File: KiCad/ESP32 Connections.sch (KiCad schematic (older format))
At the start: 1 part

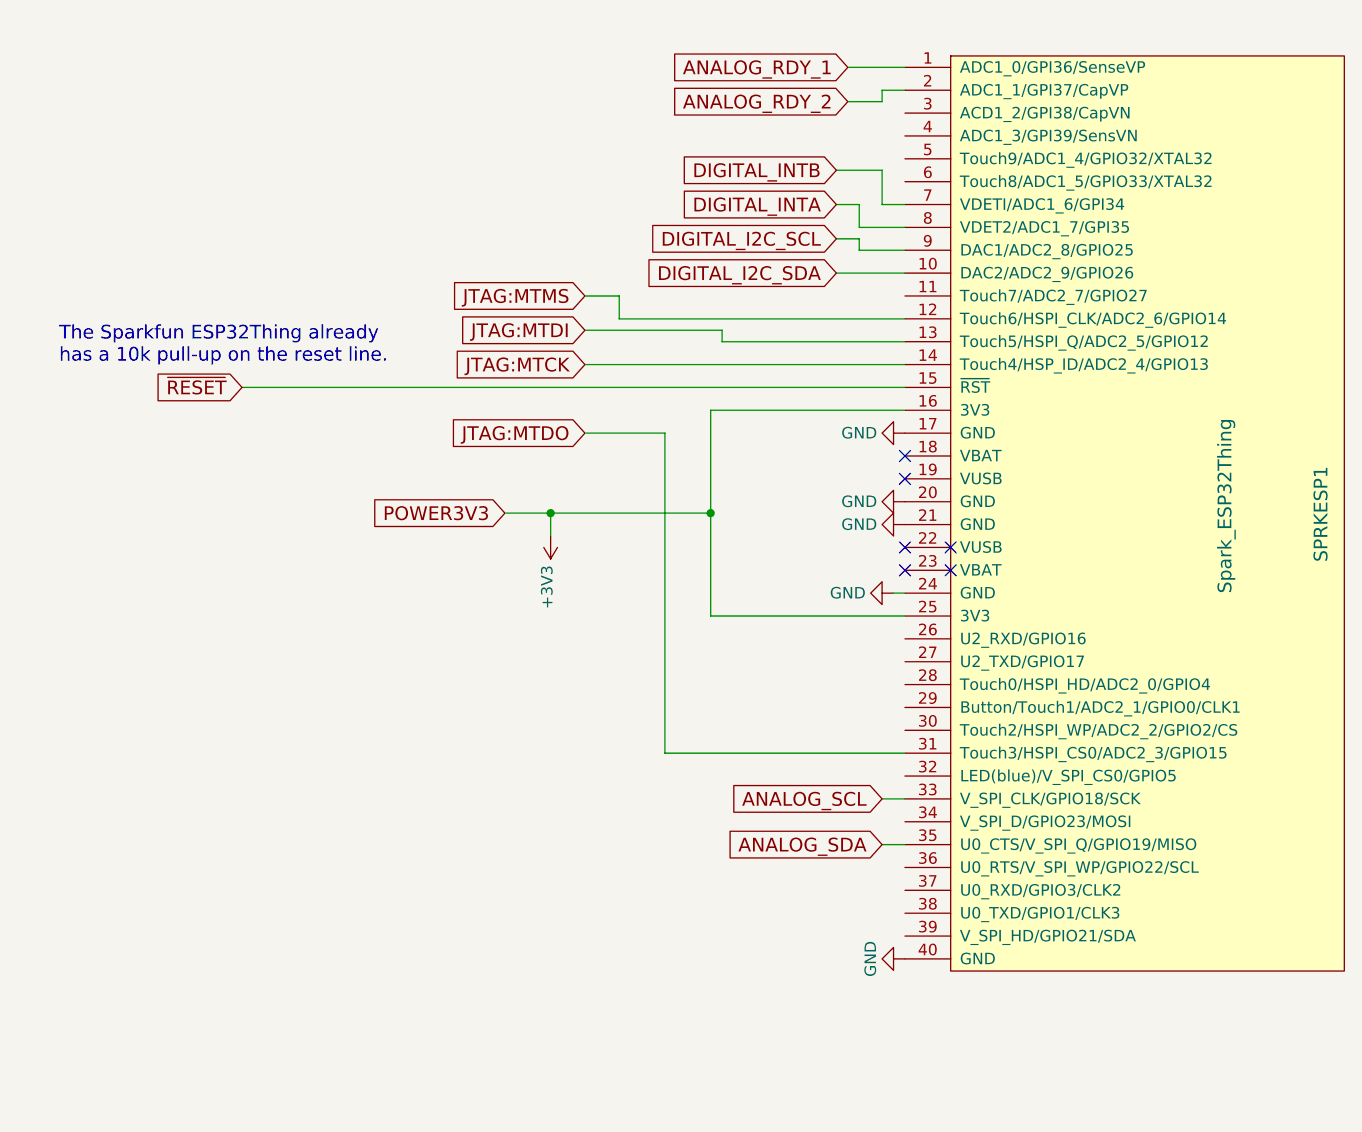
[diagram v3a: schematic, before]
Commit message: Reworked power-supply to provide 5V. Updated ESP-connections.
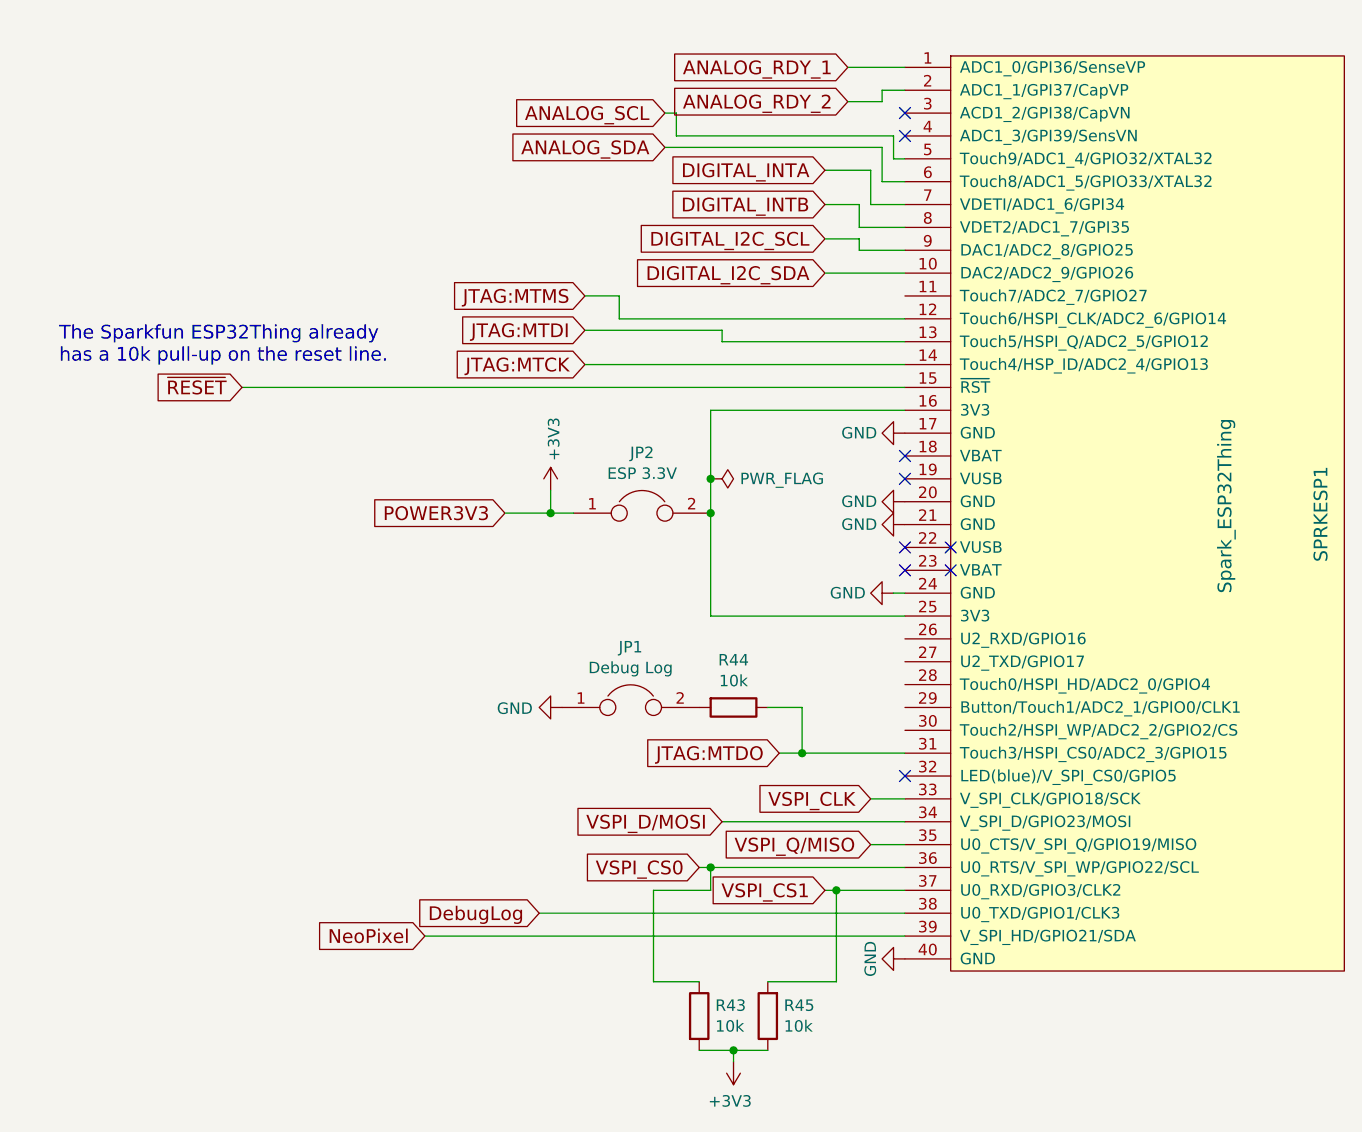
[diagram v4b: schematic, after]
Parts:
- added JP1: Debug Log, Pin_Headers:Pin_Header_Straight_1x02_Pitch2.54mm, symbol Jumper
- added JP2: ESP 3.3V, Pin_Headers:Pin_Header_Straight_1x02_Pitch2.54mm, symbol Jumper
- added R43, R44, R45: 10k, Resistors_SMD:R_0805, symbol R
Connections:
- net +3V3: now also JP2.1, R43.2, R45.1; no longer SPRKESP1.16 (3V3), SPRKESP1.25 (3V3)
- net ANALOG_SCL: now also SPRKESP1.5 (Touch9/ADC1_4/GPIO32/XTAL32); no longer SPRKESP1.33 (V_SPI_CLK/GPIO18/SCK)
- net ANALOG_SDA: now also SPRKESP1.6 (Touch8/ADC1_5/GPIO33/XTAL32); no longer SPRKESP1.35 (U0_CTS/V_SPI_Q/GPIO19/MISO)
- net DIGITAL_INTA: now also SPRKESP1.7 (VDETI/ADC1_6/GPI34); no longer SPRKESP1.8 (VDET2/ADC1_7/GPI35)
- net DIGITAL_INTB: now also SPRKESP1.8 (VDET2/ADC1_7/GPI35); no longer SPRKESP1.7 (VDETI/ADC1_6/GPI34)
- net GND: now also JP1.1
- net JTAG:MTDO: now also R44.1
- net VSPI_D/MOSI: now reaches SPRKESP1.34 (V_SPI_D/GPIO23/MOSI)
- net VSPI_CS0: now reaches SPRKESP1.36 (U0_RTS/V_SPI_WP/GPIO22/SCL)
- net VSPI_CS0: now also R43.1
- net VSPI_CS1: now reaches SPRKESP1.37 (U0_RXD/GPIO3/CLK2)
- net VSPI_CS1: now also R45.2
- net DebugLog: now reaches SPRKESP1.38 (U0_TXD/GPIO1/CLK3)
- net NeoPixel: now reaches SPRKESP1.39 (V_SPI_HD/GPIO21/SDA)
- new net: JP2.2, SPRKESP1.16 (3V3), SPRKESP1.25 (3V3)
- new net: JP1.2, R44.2
- new net VSPI_CLK: SPRKESP1.33 (V_SPI_CLK/GPIO18/SCK)
- new net VSPI_Q/MISO: SPRKESP1.35 (U0_CTS/V_SPI_Q/GPIO19/MISO)
- no-connect marks 6 -> 9
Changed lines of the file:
@@
 LIBS:SRR1260-330M
 LIBS:ADS1115IDGST
+LIBS:LM1086
 LIBS:HAP-IO-Card-cache
 EELAYER 26 0
@@
 $Descr A4 11693 8268
 encoding utf-8
-Sheet 3 6
+Sheet 3 7
 Title ""
 Date ""
@@
 Text GLabel 3800 3150 0    60   Input ~ 0
 JTAG:MTDI
-Text GLabel 3800 3600 0    60   Input ~ 0
+Text GLabel 4650 5000 0    60   Input ~ 0
 JTAG:MTDO
 Text GLabel 3800 3300 0    60   Input ~ 0
 JTAG:MTCK
-Wire Wire Line
-	3800 3300 5200 3300
 Text GLabel 3800 3000 0    60   Input ~ 0
 JTAG:MTMS
-Wire Wire Line
-	3800 3150 4400 3150
-Wire Wire Line
-	4400 3150 4400 3200
-Wire Wire Line
-	4400 3200 5200 3200
-Wire Wire Line
-	5200 3100 3950 3100
-Wire Wire Line
-	3950 3100 3950 3000
-Wire Wire Line
-	3950 3000 3800 3000
-Wire Wire Line
-	4150 5000 5200 5000
-Wire Wire Line
-	4150 3600 3800 3600
-Wire Wire Line
-	2300 3400 5200 3400
-Wire Wire Line
-	4150 5000 4150 3600
 NoConn ~ 5200 4200
 NoConn ~ 5200 4100
-Wire Wire Line
-	5200 3500 4350 3500
-Wire Wire Line
-	4350 3500 4350 4400
-Wire Wire Line
-	3450 3950 4350 3950
-Wire Wire Line
-	4350 4400 5200 4400
-Connection ~ 4350 3950
 Text GLabel 2300 3400 0    60   Input ~ 0
 ~RESET
-Text GLabel 5100 5400 0    60   Input ~ 0
+Text GLabel 4150 2350 0    60   Input ~ 0
 ANALOG_SDA
-Text GLabel 5100 5200 0    60   Input ~ 0
+Text GLabel 4150 2200 0    60   Input ~ 0
 ANALOG_SCL
-Text GLabel 4900 2600 0    60   Input ~ 0
+Text GLabel 4850 2450 0    60   Input ~ 0
 DIGITAL_INTA
-Text GLabel 4900 2450 0    60   Input ~ 0
+Text GLabel 4850 2600 0    60   Input ~ 0
 DIGITAL_INTB
-Text GLabel 4900 2750 0    60   Input ~ 0
+Text GLabel 4850 2750 0    60   Input ~ 0
 DIGITAL_I2C_SCL
-Text GLabel 4900 2900 0    60   Input ~ 0
+Text GLabel 4850 2900 0    60   Input ~ 0
 DIGITAL_I2C_SDA
-Wire Wire Line
-	5100 5200 5200 5200
-Wire Wire Line
-	5100 5400 5200 5400
-Wire Wire Line
-	4900 2900 5200 2900
-Wire Wire Line
-	4900 2750 5000 2750
-Wire Wire Line
-	5000 2750 5000 2800
-Wire Wire Line
-	5000 2800 5200 2800
-Wire Wire Line
-	5200 2700 5000 2700
-Wire Wire Line
-	5000 2700 5000 2600
-Wire Wire Line
-	5000 2600 4900 2600
-Wire Wire Line
-	4900 2450 5100 2450
-Wire Wire Line
-	5100 2450 5100 2600
-Wire Wire Line
-	5100 2600 5200 2600
-Wire Wire Line
-	5200 4300 5150 4300
 Text Notes 1500 3300 0    60   ~ 0
 The Sparkfun ESP32Thing already\nhas a 10k pull-up on the reset line.
 Text GLabel 4950 2000 0    60   Input ~ 0
 ANALOG_RDY_1
-Wire Wire Line
-	4950 2000 5200 2000
 Text GLabel 4950 2150 0    60   Input ~ 0
 ANALOG_RDY_2
-Wire Wire Line
-	4950 2150 5100 2150
-Wire Wire Line
-	5100 2150 5100 2100
-Wire Wire Line
-	5100 2100 5200 2100
 Text GLabel 3450 3950 0    60   Input ~ 0
 POWER3V3
@@
 L +3V3 #PWR047
 U 1 1 592C50A9
-P 3650 4050
-F 0 "#PWR047" H 3650 3900 50  0001 C CNN
-F 1 "+3V3" V 3665 4178 50  0000 L CNN
-F 2 "" H 3650 4050 50  0001 C CNN
-F 3 "" H 3650 4050 50  0001 C CNN
-	1    3650 4050
+P 3650 3850
+F 0 "#PWR047" H 3650 3700 50  0001 C CNN
+F 1 "+3V3" V 3665 3978 50  0000 L CNN
+F 2 "" H 3650 3850 50  0001 C CNN
+F 3 "" H 3650 3850 50  0001 C CNN
+	1    3650 3850
+	1    0    0    -1
+$EndComp
+Text GLabel 4300 5500 0    60   Input ~ 0
+VSPI_CS0
+Text GLabel 5050 5200 0    60   Input ~ 0
+VSPI_CLK
+Text GLabel 4400 5300 0    60   Input ~ 0
+VSPI_D/MOSI
+Text GLabel 5050 5400 0    60   Input ~ 0
+VSPI_Q/MISO
+$Comp
+L GND #PWR048
+U 1 1 5924796B
+P 3700 4800
+F 0 "#PWR048" H 3700 4550 50  0001 C CNN
+F 1 "GND" V 3705 4672 50  0000 R CNN
+F 2 "" H 3700 4800 50  0001 C CNN
+F 3 "" H 3700 4800 50  0001 C CNN
+	1    3700 4800
+	0    1    1    0
+$EndComp
+NoConn ~ 5200 2300
+NoConn ~ 5200 2200
+$Comp
+L R R43
+U 1 1 592490B8
+P 4300 6150
+F 0 "R43" H 4370 6196 50  0000 L CNN
+F 1 "10k" H 4370 6105 50  0000 L CNN
+F 2 "Resistors_SMD:R_0805" V 4230 6150 50  0001 C CNN
+F 3 "" H 4300 6150 50  0001 C CNN
+	1    4300 6150
+	1    0    0    -1
+$EndComp
+$Comp
+L +3V3 #PWR049
+U 1 1 5924911C
+P 4450 6350
+F 0 "#PWR049" H 4450 6200 50  0001 C CNN
+F 1 "+3V3" H 4465 6523 50  0000 C CNN
+F 2 "" H 4450 6350 50  0001 C CNN
+F 3 "" H 4450 6350 50  0001 C CNN
+	1    4450 6350
 	-1   0    0    1
 $EndComp
-Wire Wire Line
-	3650 3950 3650 4050
+Text GLabel 4850 5600 0    60   Input ~ 0
+VSPI_CS1
+Wire Wire Line
+	3800 3300 5200 3300
+Wire Wire Line
+	3800 3150 4400 3150
+Wire Wire Line
+	4400 3150 4400 3200
+Wire Wire Line
+	4400 3200 5200 3200
+Wire Wire Line
+	5200 3100 3950 3100
+Wire Wire Line
+	3950 3100 3950 3000
+Wire Wire Line
+	3950 3000 3800 3000
+Wire Wire Line
+	2300 3400 5200 3400
+Wire Wire Line
+	5200 3500 4350 3500
+Wire Wire Line
+	4350 4400 5200 4400
+Wire Wire Line
+	5050 5200 5200 5200
+Wire Wire Line
+	5050 5400 5200 5400
+Wire Wire Line
+	4850 2900 5200 2900
+Wire Wire Line
+	4850 2750 5000 2750
+Wire Wire Line
+	5000 2750 5000 2800
+Wire Wire Line
+	5000 2800 5200 2800
+Wire Wire Line
+	5200 2700 5000 2700
+Wire Wire Line
+	5000 2700 5000 2600
+Wire Wire Line
+	5000 2600 4850 2600
+Wire Wire Line
+	4850 2450 5050 2450
+Wire Wire Line
+	5050 2450 5050 2600
+Wire Wire Line
+	5050 2600 5200 2600
+Wire Wire Line
+	5200 4300 5150 4300
+Wire Wire Line
+	4950 2000 5200 2000
+Wire Wire Line
+	4950 2150 5100 2150
+Wire Wire Line
+	5100 2150 5100 2100
+Wire Wire Line
+	5100 2100 5200 2100
+Wire Wire Line
+	3650 3950 3650 3850
 Connection ~ 3650 3950
+Wire Wire Line
+	4650 5000 4750 5000
+Wire Wire Line
+	4750 5000 5200 5000
+Wire Wire Line
+	4600 4800 4750 4800
+Wire Wire Line
+	4750 4800 4750 5000
+Connection ~ 4750 5000
+Wire Wire Line
+	3600 5700 5200 5700
+Wire Wire Line
+	4150 2350 5100 2350
+Wire Wire Line
+	5100 2350 5100 2500
+Wire Wire Line
+	5100 2500 5200 2500
+Wire Wire Line
+	4150 2200 4200 2200
+Wire Wire Line
+	4200 2200 4200 2300
+Wire Wire Line
+	4200 2300 5150 2300
+Wire Wire Line
+	5150 2300 5150 2400
+Wire Wire Line
+	5150 2400 5200 2400
+Wire Wire Line
+	4400 5300 5200 5300
+$Comp
+L R R45
+U 1 1 59249210
+P 4600 6150
+F 0 "R45" H 4530 6104 50  0000 R CNN
+F 1 "10k" H 4530 6195 50  0000 R CNN
+F 2 "Resistors_SMD:R_0805" V 4530 6150 50  0001 C CNN
+F 3 "" H 4600 6150 50  0001 C CNN
+	1    4600 6150
+	-1   0    0    1
+$EndComp
+Text GLabel 3100 5800 0    60   Input ~ 0
+NeoPixel
+Wire Wire Line
+	4300 5500 4350 5500
+Wire Wire Line
+	4350 5500 5200 5500
+Wire Wire Line
+	4850 5600 4900 5600
+Wire Wire Line
+	4900 5600 5200 5600
+Wire Wire Line
+	4300 6300 4450 6300
+Wire Wire Line
+	4450 6300 4600 6300
+Wire Wire Line
+	4450 6350 4450 6300
+Connection ~ 4450 6300
+Wire Wire Line
+	4600 6000 4900 6000
+Wire Wire Line
+	4900 6000 4900 5600
+Connection ~ 4900 5600
+Wire Wire Line
+	4300 6000 4100 6000
+Wire Wire Line
+	4100 6000 4100 5600
+Wire Wire Line
+	4100 5600 4350 5600
+Wire Wire Line
+	4350 5600 4350 5500
+Connection ~ 4350 5500
+NoConn ~ 5200 5100
+$Comp
+L Jumper JP2
+U 1 1 59249D8C
+P 4050 3950
+F 0 "JP2" H 4050 4214 50  0000 C CNN
+F 1 "ESP 3.3V" H 4050 4123 50  0000 C CNN
+F 2 "Pin_Headers:Pin_Header_Straight_1x02_Pitch2.54mm" H 4050 3950 50  0001 C CNN
+F 3 "" H 4050 3950 50  0001 C CNN
+	1    4050 3950
+	1    0    0    -1
+$EndComp
+Wire Wire Line
+	3450 3950 3650 3950
+Wire Wire Line
+	3650 3950 3750 3950
+Wire Wire Line
+	4350 3500 4350 3800
+Wire Wire Line
+	4350 3800 4350 3950
+Wire Wire Line
+	4350 3950 4350 4400
+Connection ~ 4350 3950
+Text GLabel 3600 5700 0    60   Input ~ 0
+DebugLog
+$Comp
+L R R44
+U 1 1 5924AA09
+P 4450 4800
+F 0 "R44" V 4243 4800 50  0000 C CNN
+F 1 "10k" V 4334 4800 50  0000 C CNN
+F 2 "Resistors_SMD:R_0805" V 4380 4800 50  0001 C CNN
+F 3 "" H 4450 4800 50  0001 C CNN
+	1    4450 4800
+	0    1    1    0
+$EndComp
+$Comp
+L Jumper JP1
+U 1 1 5924AABC
+P 4000 4800
+F 0 "JP1" H 4000 5064 50  0000 C CNN
+F 1 "Debug Log" H 4000 4973 50  0000 C CNN
+F 2 "Pin_Headers:Pin_Header_Straight_1x02_Pitch2.54mm" H 4000 4800 50  0001 C CNN
+F 3 "" H 4000 4800 50  0001 C CNN
+	1    4000 4800
+	1    0    0    -1
+$EndComp
+Wire Wire Line
+	3100 5800 5200 5800
+$Comp
+L PWR_FLAG #FLG050
+U 1 1 5924FE9E
+P 4350 3800
+F 0 "#FLG050" H 4350 3875 50  0001 C CNN
+F 1 "PWR_FLAG" V 4350 3928 50  0000 L CNN
+F 2 "" H 4350 3800 50  0001 C CNN
+F 3 "" H 4350 3800 50  0001 C CNN
+	1    4350 3800
+	0    1    1    0
+$EndComp
+Connection ~ 4350 3800
 $EndSCHEMATC

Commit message: More work
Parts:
- JP301: renamed from JP1; value Debug Log -> Debug Log Disable
- renumbered JP2 to JP302, R43 to R301, R45 to R302, R44 to R303, SPRKESP1 to SPRKESP301
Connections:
- net VSPI_CS1: now also SPRKESP301.28 (Touch0/HSPI_HD/ADC2_0/GPIO4); no longer SPRKESP301.37 (U0_RXD/GPIO3/CLK2)
- net 5V_I/O_2: now reaches SPRKESP301.11 (Touch7/ADC2_7/GPIO27)
- net GPIO16/UART2_RX: now reaches SPRKESP301.26 (U2_RXD/GPIO16)
- net GPIO17/UART2_TX: now reaches SPRKESP301.27 (U2_TXD/GPIO17)
- net GPIO0/Button: now reaches SPRKESP301.29 (Button/Touch1/ADC2_1/GPIO0/CLK1)
- net GPI38: now reaches SPRKESP301.3 (ACD1_2/GPI38/CapVN)
- net 5V_I/O_Enable: now reaches SPRKESP301.30 (Touch2/HSPI_WP/ADC2_2/GPIO2/CS)
- net GPIO5/LED: now reaches SPRKESP301.32 (LED(blue)/V_SPI_CS0/GPIO5)
- net GPI39: now reaches SPRKESP301.4 (ADC1_3/GPI39/SensVN)
- net DebugLog renamed GPIO/1UART0_TX
- net NeoPixel renamed 5V_I/O_1
- new net GPIO3/UART0_RX: SPRKESP301.37 (U0_RXD/GPIO3/CLK2)
- no-connect marks 9 -> 6
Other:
- moved on the sheet: JP301, R301, R302, R303
